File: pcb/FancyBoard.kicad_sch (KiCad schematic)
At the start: 171 parts, among them J1 Conn_01x02_Socket, SW1 SW_Push_45deg, SW10 SW_Push_45deg, SW11 SW_Push_45deg, SW12 SW_Push_45deg, SW13 SW_Push_45deg, SW14 SW_Push_45deg, SW15 SW_Push_45deg, SW16 SW_Push_45deg, SW17 SW_Push_45deg, SW18 SW_Push_45deg, SW19 SW_Push_45deg, SW2 SW_Push_45deg, SW20 SW_Push_45deg, SW21 SW_Push_45deg, SW22 SW_Push_45deg, SW23 SW_Push_45deg, SW24 SW_Push_45deg, SW25 SW_Push_45deg, SW26 SW_Push_45deg, SW27 SW_Push_45deg, SW28 SW_Push_45deg, SW29 SW_Push_45deg, SW3 SW_Push_45deg, SW30 SW_Push_45deg, SW31 SW_Push_45deg, SW32 SW_Push_45deg, SW33 SW_Push_45deg, SW34 SW_Push_45deg, SW35 SW_Push_45deg, SW36 SW_Push_45deg, SW37 SW_Push_45deg, SW38 SW_Push_45deg, SW39 SW_Push_45deg, SW4 SW_Push_45deg, SW40 SW_Push_45deg, SW41 SW_Push_45deg, SW42 SW_Push_45deg, SW43 SW_Push_45deg, SW44 SW_Push_45deg, SW45 SW_Push_45deg, SW46 SW_Push_45deg, SW47 SW_Push_45deg, SW48 SW_Push_45deg, SW49 SW_Push_45deg, SW5 SW_Push_45deg, SW50 SW_Push_45deg, SW51 SW_Push_45deg, SW52 SW_Push_45deg, SW53 SW_Push_45deg, SW54 SW_Push_45deg, SW55 SW_Push_45deg, SW56 RotaryEncoder_Switch, SW57 RotaryEncoder_Switch, SW58 SW_SPDT, SW6 SW_Push_45deg, SW7 SW_Push_45deg, SW70 SW_Push_45deg, SW71 SW_Push_45deg, SW72 SW_Push_45deg, SW73 SW_Push_45deg, SW74 SW_Push_45deg, SW75 SW_Push_45deg, SW76 SW_Push_45deg, SW77 SW_Push_45deg, SW78 SW_Push_45deg, SW79 SW_Push_45deg, SW8 SW_Push_45deg, SW80 SW_Push_45deg, SW81 SW_Push_45deg, SW82 SW_Push_45deg, SW83 SW_Push_45deg, SW84 SW_Push_45deg, SW85 SW_Push_45deg, SW86 SW_Push_45deg, SW87 SW_Push_45deg, SW88 SW_Push_45deg, SW89 SW_Push_45deg, SW9 SW_Push_45deg, SW90 SW_Push_45deg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

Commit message: schematic done
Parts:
- added R10, R11, R6, R7, R8, R9: 10K, symbol Device:R
- added R2, R3, R4, R5: 4.7K, symbol Device:R
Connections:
- net +3V3: now also R1.1, R10.1, R11.1, R2.1, R3.1, R4.1, R5.1, R6.1, R7.1, R8.1, R9.1; no longer SW58.1 (A)
- net GND: now also SW58.2 (B); no longer R1.2, SW58.3 (C), U2.5 (RES)
- net IO15: now also R8.2
- net IO16: now also R1.2, U2.5 (RES); no longer R1.1
- net IO18: now also SW58.1 (A), R10.2, R7.2; no longer SW58.2 (B)
- net IO19: now also R6.2
- net IO20: now also R9.2
- net SCL: now also R3.2, R5.2
- net SDA: now also R2.2, R4.2
- new net IO9: R11.2, SW58.3 (C)
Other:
- moved on the sheet: C1, C2, C5, C6, D1, D10, D11, D12, D13, D14, D15, D16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

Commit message: mostly done pcb
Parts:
- removed D69: 1N4148W, Diode_SMD:D_SOD-123, symbol Diode:1N4148W
- removed SW83, SW93: SW_Push_45deg, symbol Switch:SW_Push_45deg
- added SW78: SW_Push_45deg, Kailh_PG1353_Hotswap:Kailh-PG1353-Hotswap-1U, symbol Switch:SW_Push_45deg
- C1, C2, C5, C6: footprint (none) -> Capacitor_SMD:C_0603_1608Metric
- J1: footprint (none) -> Connector_JST:JST_PH_B2B-PH-K_1x02_P2.00mm_Vertical
- R1, R10, R11, R2, R3, R4, R5, R6, R7, R8, R9: footprint (none) -> Resistor_SMD:R_0603_1608Metric
- SW1, SW14, SW29, SW42: footprint (none) -> Kailh_PG1353_Hotswap:Kailh-PG1353-Hotswap-1.5U
- SW10, SW11, SW12, SW13, SW15, SW16, SW17, SW18, SW19, SW2, SW20, SW21, SW22, SW23, SW24, SW25, SW26, SW27, SW3, SW30, SW31, SW32, SW33, SW34, SW35, SW36, SW37, SW38, SW39, SW4, SW40, SW41, SW44, SW45, SW46, SW47, SW48, SW49, SW5, SW50, SW51, SW52, SW53, SW54, SW6, SW7, SW8, SW9: footprint (none) -> Kailh_PG1353_Hotswap:Kailh-PG1353-Hotswap-1U
- SW28: footprint (none) -> Kailh_PG1353_Hotswap:Kailh-PG1353-Hotswap-2U
- SW43: footprint (none) -> Kailh_PG1353_Hotswap:Kailh-PG1353-Hotswap-1.75U
- SW55: footprint (none) -> Kailh_PG1353_Hotswap:Kailh-PG1353-Hotswap-2.25U
- SW56: renamed from SW70; footprint (none) -> Kailh_PG1353_Hotswap:Kailh-PG1353-Hotswap-2.25U
- SW57: renamed from SW71; footprint (none) -> Kailh_PG1353_Hotswap:Kailh-PG1353-Hotswap-1U
- SW58: renamed from SW72; footprint (none) -> Kailh_PG1353_Hotswap:Kailh-PG1353-Hotswap-1U
- SW59: renamed from SW73; footprint (none) -> Kailh_PG1353_Hotswap:Kailh-PG1353-Hotswap-1U
- SW60: renamed from SW74; footprint (none) -> Kailh_PG1353_Hotswap:Kailh-PG1353-Hotswap-1U
- SW61: renamed from SW75; footprint (none) -> Kailh_PG1353_Hotswap:Kailh-PG1353-Hotswap-1U
- SW62: renamed from SW76; footprint (none) -> Kailh_PG1353_Hotswap:Kailh-PG1353-Hotswap-1U
- SW63: renamed from SW77; footprint (none) -> Kailh_PG1353_Hotswap:Kailh-PG1353-Hotswap-1U
- SW64: renamed from SW78; footprint (none) -> Kailh_PG1353_Hotswap:Kailh-PG1353-Hotswap-1U
- SW65: renamed from SW79; footprint (none) -> Kailh_PG1353_Hotswap:Kailh-PG1353-Hotswap-1U
- SW66: renamed from SW80; footprint (none) -> Kailh_PG1353_Hotswap:Kailh-PG1353-Hotswap-1U
- SW67: renamed from SW81; footprint (none) -> Kailh_PG1353_Hotswap:Kailh-PG1353-Hotswap-1.75U
- SW68: renamed from SW82; footprint (none) -> Kailh_PG1353_Hotswap:Kailh-PG1353-Hotswap-1U
- SW69: renamed from SW84; footprint (none) -> Kailh_PG1353_Hotswap:Kailh-PG1353-Hotswap-1.25U
- SW70: renamed from SW85; footprint (none) -> Kailh_PG1353_Hotswap:Kailh-PG1353-Hotswap-1.25U
- SW71: renamed from SW86; footprint (none) -> Kailh_PG1353_Hotswap:Kailh-PG1353-Hotswap-1.25U
- SW72: renamed from SW87; footprint (none) -> Kailh_PG1353_Hotswap:Kailh-PG1353-Hotswap-6.25U
- SW73: renamed from SW88; footprint (none) -> Kailh_PG1353_Hotswap:Kailh-PG1353-Hotswap-1U
- SW74: renamed from SW89; footprint (none) -> Kailh_PG1353_Hotswap:Kailh-PG1353-Hotswap-1U
- SW75: renamed from SW90; footprint (none) -> Kailh_PG1353_Hotswap:Kailh-PG1353-Hotswap-1U
- SW76: renamed from SW91; footprint (none) -> Kailh_PG1353_Hotswap:Kailh-PG1353-Hotswap-1U
- SW77: renamed from SW92; footprint (none) -> Kailh_PG1353_Hotswap:Kailh-PG1353-Hotswap-1U
- SW93: renamed from SW56; footprint (none) -> Rotary_Encoder:RotaryEncoder_Alps_EC11E-Switch_Vertical_H20mm
- SW94: renamed from SW57; footprint (none) -> Rotary_Encoder:RotaryEncoder_Alps_EC11E-Switch_Vertical_H20mm
- SW95: renamed from SW58; footprint (none) -> SS-12D00:SS12-D00
- U1: footprint (none) -> nice!nanov2:nice!nanov2
- U2: footprint (none) -> ST7789_Module:ST7789_Module
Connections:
- net COL10: now also SW78.1
- net GND: now also U1.1 (GND), U1.22 (3.3V), U1.5 (GND); no longer U1.26 (3.3V)
- net IO14: now also R8.2, SW94.A, U1.16 (IO14); no longer SW93.S1, U1.18 (IO14)
- net IO15: now also R1.2, U1.17 (IO15), U2.5 (RES); no longer R8.2, SW94.A, U1.19 (IO15)
- net IO16: now also SW93.S1, U1.15 (IO16); no longer R1.2, U1.20 (IO16), U2.5 (RES)
- net IO18: now also U1.18 (IO18); no longer U1.22 (IO18)
- net IO19: now also U1.19 (IO19); no longer U1.23 (IO19)
- net IO20: now also U1.20 (IO20); no longer U1.24 (IO20)
- net IO21: now also U1.21 (IO21); no longer U1.25 (IO21)
- net at D79.2 (A): now also SW78.2
- net at J1.1 (Pin_1): now also U1.25 (BATT+); no longer U1.29 (BATT+)
- net at J1.2 (Pin_2): now also U1.24 (GND); no longer U1.28 (GND)
- no-connect marks 17 -> 18

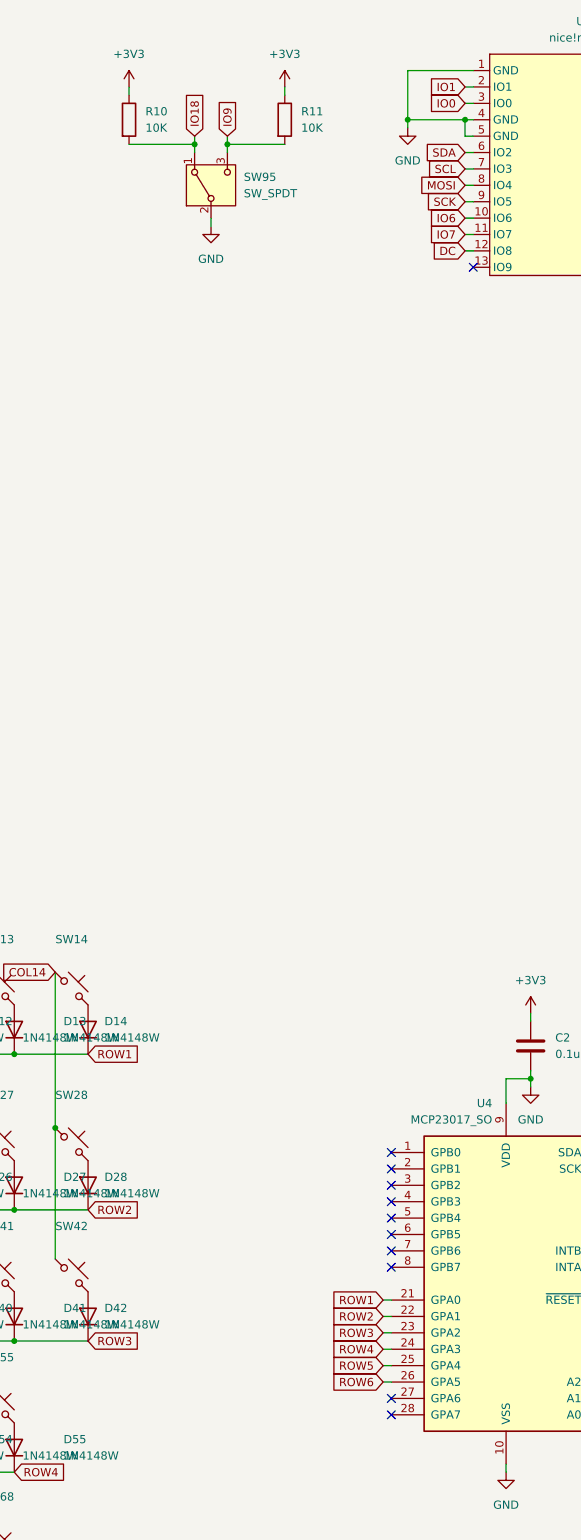
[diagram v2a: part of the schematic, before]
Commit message: mostly done routing
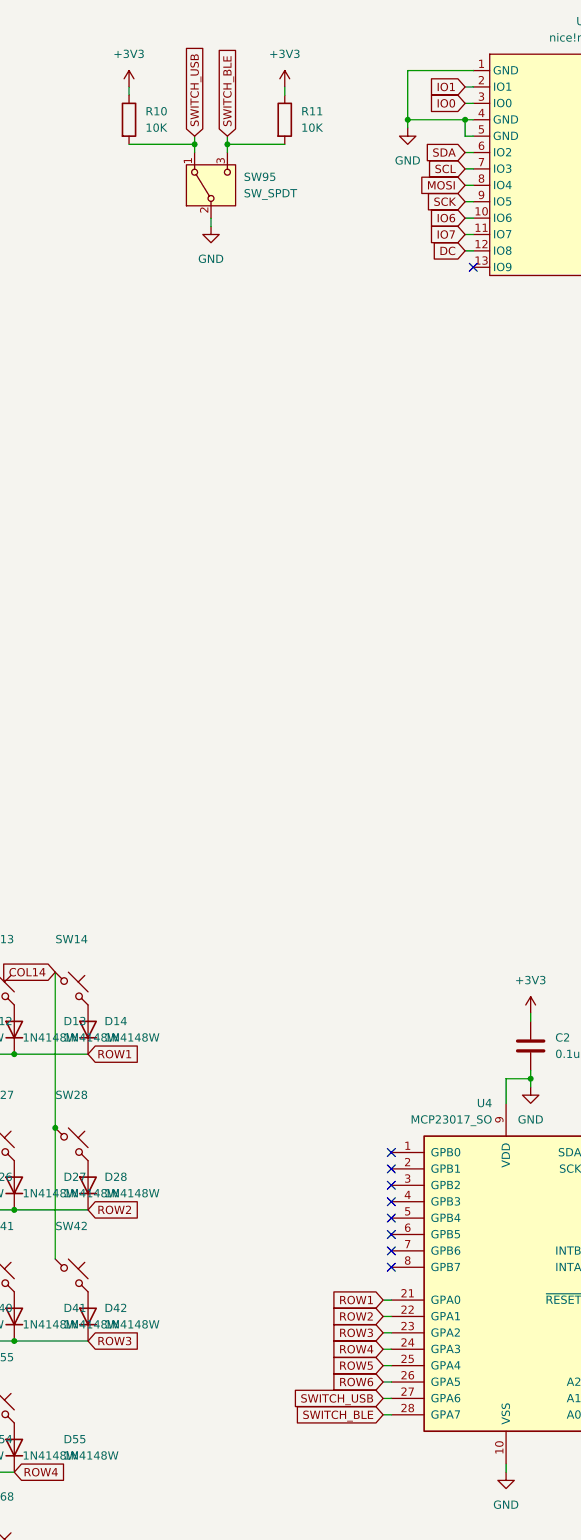
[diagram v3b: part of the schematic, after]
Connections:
- net IO9 is gone; now on net SWITCH_BLE: R11.2, SW95.3 (C)
- net IO18: no longer R10.2, SW95.1 (A)
- net SWITCH_USB: now reaches U4.27 (GPA6)
- net SWITCH_USB: now also R10.2, SW95.1 (A)
- net SWITCH_BLE: now reaches U4.28 (GPA7)
- no-connect marks 18 -> 16
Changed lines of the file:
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@@
 	)
 	(no_connect
-		(at 215.9 231.14)
-	)
-	(no_connect
-		(at 215.9 228.6)
-	)
-	(no_connect
 		(at 215.9 205.74)
 	)
@@
 	(wire
 		(pts
+			(xy 214.63 231.14) (xy 215.9 231.14)
+		)
+		(stroke
+			(width 0)
+			(type default)
+		)
+	)
+	(wire
+		(pts
 			(xy 124.46 175.26) (xy 134.62 175.26)
 		)
@@
 	(wire
 		(pts
+			(xy 262.89 53.34) (xy 264.16 53.34)
+		)
+		(stroke
+			(width 0)
+			(type default)
+		)
+	)
+	(wire
+		(pts
 			(xy 309.88 121.92) (xy 309.88 123.19)
 		)
@@
 	(wire
 		(pts
-			(xy 262.89 53.34) (xy 264.16 53.34)
-		)
-		(stroke
-			(width 0)
-			(type default)
-		)
-	)
-	(wire
-		(pts
 			(xy 328.93 39.37) (xy 328.93 40.64)
 		)
@@
 		)
 	)
+	(wire
+		(pts
+			(xy 214.63 228.6) (xy 215.9 228.6)
+		)
+		(stroke
+			(width 0)
+			(type default)
+		)
+	)
 	(global_label "COL3"
 		(shape input)
@@
 		)
 	)
-	(global_label "IO18"
+	(global_label "SWITCH_USB"
 		(shape input)
 		(at 185.42 33.02 90)
@@
 		)
 		(property "Intersheetrefs" "${INTERSHEET_REFS}"
-			(at 185.42 25.6805 90)
+			(at 185.42 18.4234 90)
 			(effects
 				(font
@@
 		)
 	)
+	(global_label "SWITCH_USB"
+		(shape input)
+		(at 214.63 228.6 180)
+		(fields_autoplaced yes)
+		(effects
+			(font
+				(size 1.27 1.27)
+			)
+			(justify right)
+		)
+		(property "Intersheetrefs" "${INTERSHEET_REFS}"
+			(at 200.0334 228.6 0)
+			(effects
+				(font
+					(size 1.27 1.27)
+				)
+				(justify right)
+				(hide yes)
+			)
+		)
+	)
 	(global_label "ROW5"
 		(shape input)
@@
 		)
 	)
+	(global_label "SWITCH_BLE"
+		(shape input)
+		(at 214.63 231.14 180)
+		(fields_autoplaced yes)
+		(effects
+			(font
+				(size 1.27 1.27)
+			)
+			(justify right)
+		)
+		(property "Intersheetrefs" "${INTERSHEET_REFS}"
+			(at 200.3963 231.14 0)
+			(effects
+				(font
+					(size 1.27 1.27)
+				)
+				(justify right)
+				(hide yes)
+			)
+		)
+	)
 	(global_label "IO0"
 		(shape input)
@@
 		)
 	)
-	(global_label "IO10"
-		(shape input)
-		(at 264.16 53.34 0)
-		(fields_autoplaced yes)
-		(effects
-			(font
-				(size 1.27 1.27)
-			)
-			(justify left)
-		)
-		(property "Intersheetrefs" "${INTERSHEET_REFS}"
-			(at 271.4995 53.34 0)
-			(effects
-				(font
-					(size 1.27 1.27)
-				)
-				(justify left)
-				(hide yes)
-			)
-		)
-	)
-	(global_label "IO9"
+	(global_label "SWITCH_BLE"
 		(shape input)
 		(at 190.5 33.02 90)
@@
 		)
 		(property "Intersheetrefs" "${INTERSHEET_REFS}"
-			(at 190.5 26.89 90)
+			(at 190.5 18.7863 90)
 			(effects
 				(font
@@
 				(hide yes)
 			)
+		)
+	)
+	(global_label "IO10"
+		(shape input)
+		(at 264.16 53.34 0)
+		(fields_autoplaced yes)
+		(effects
+			(font
+				(size 1.27 1.27)
+			)
+			(justify left)
+		)
+		(property "Intersheetrefs" "${INTERSHEET_REFS}"
+			(at 271.4995 53.34 0)
+			(effects
+				(font
+					(size 1.27 1.27)
+				)
+				(justify left)
+				(hide yes)
+			)

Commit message: pcb done?
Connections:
- net +3V3: now also U1.22 (3.3V)
- net GND: no longer U1.22 (3.3V)
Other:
- moved on the sheet: C1
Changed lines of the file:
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@@
 	)
 	(junction
-		(at 281.94 33.02)
-		(diameter 0)
-		(color 0 0 0 0)
-	)
-	(junction
 		(at 107.95 186.69)
 		(diameter 0)
@@
 	)
 	(junction
+		(at 279.4 33.02)
+		(diameter 0)
+		(color 0 0 0 0)
+	)
+	(junction
 		(at 332.74 228.6)
 		(diameter 0)
@@
 	(wire
 		(pts
-			(xy 281.94 33.02) (xy 281.94 31.75)
+			(xy 279.4 33.02) (xy 279.4 31.75)
 		)
 		(stroke
@@
 	(wire
 		(pts
+			(xy 279.4 43.18) (xy 279.4 41.91)
+		)
+		(stroke
+			(width 0)
+			(type default)
+		)
+	)
+	(wire
+		(pts
 			(xy 262.89 38.1) (xy 264.16 38.1)
 		)
@@
 	(wire
 		(pts
-			(xy 281.94 33.02) (xy 281.94 34.29)
+			(xy 279.4 33.02) (xy 279.4 34.29)
 		)
 		(stroke
@@
 	(wire
 		(pts
-			(xy 262.89 33.02) (xy 281.94 33.02)
+			(xy 262.89 33.02) (xy 279.4 33.02)
 		)
 		(stroke
@@
 	(wire
 		(pts
-			(xy 281.94 22.86) (xy 281.94 24.13)
-		)
-		(stroke
-			(width 0)
-			(type default)
-		)
-	)
-	(wire
-		(pts
 			(xy 185.42 33.02) (xy 185.42 34.29)
 		)
@@
 	)
 	(symbol
+		(lib_id "power:+3V3")
+		(at 279.4 31.75 0)
+		(mirror y)
+		(unit 1)
+		(exclude_from_sim no)
+		(in_bom yes)
+		(on_board yes)
+		(dnp no)
+		(property "Reference" "#PWR035"
+			(at 279.4 35.56 0)
+			(effects
+				(font
+					(size 1.27 1.27)
+				)
+				(hide yes)
+			)
+		)
+		(property "Value" "+3V3"
+			(at 279.4 26.67 0)
+			(effects
+				(font
+					(size 1.27 1.27)
+				)
+			)
+		)
+		(property "Footprint" ""
+			(at 279.4 31.75 0)
+			(effects
+				(font
+					(size 1.27 1.27)
+				)
+				(hide yes)
+			)
+		)
+		(property "Datasheet" ""
+			(at 279.4 31.75 0)
+			(effects
+				(font
+					(size 1.27 1.27)
+				)
+				(hide yes)
+			)
+		)
+		(property "Description" "Power symbol creates a global label with name \"+3V3\""
+			(at 279.4 31.75 0)
+			(effects
+				(font
+					(size 1.27 1.27)
+				)
+				(hide yes)
+			)
+		)
+		(pin "1"
+		)
+		(instances
+			(project "FancyBoard"
+				(path "/5df634be-7204-4854-853b-7c7d64057627"
+					(reference "#PWR035")
+					(unit 1)
+				)
+			)
+		)
+	)
+	(symbol
 		(lib_id "Diode:1N4148W")
 		(at 91.44 278.13 90)
@@
 	)
 	(symbol
-		(lib_id "power:+3V3")
-		(at 281.94 22.86 0)
-		(unit 1)
-		(exclude_from_sim no)
-		(in_bom yes)
-		(on_board yes)
-		(dnp no)
-		(property "Reference" "#PWR019"
-			(at 281.94 26.67 0)
-			(effects
-				(font
-					(size 1.27 1.27)
-				)
-				(hide yes)
-			)
-		)
-		(property "Value" "+3V3"
-			(at 281.432 18.796 0)
-			(effects
-				(font
-					(size 1.27 1.27)
-				)
-			)
-		)
-		(property "Footprint" ""
-			(at 281.94 22.86 0)
-			(effects
-				(font
-					(size 1.27 1.27)
-				)
-				(hide yes)
-			)
-		)
-		(property "Datasheet" ""
-			(at 281.94 22.86 0)
-			(effects
-				(font
-					(size 1.27 1.27)
-				)
-				(hide yes)
-			)
-		)
-		(property "Description" "Power symbol creates a global label with name \"+3V3\""
-			(at 281.94 22.86 0)
-			(effects
-				(font
-					(size 1.27 1.27)
-				)
-				(hide yes)
-			)
-		)
-		(pin "1"
-		)
-		(instances
-			(project "FancyBoard"
-				(path "/5df634be-7204-4854-853b-7c7d64057627"
-					(reference "#PWR019")
-					(unit 1)
-				)
-			)
-		)
-	)
-	(symbol
 		(lib_id "Switch:SW_Push_45deg")
 		(at 110.49 229.87 0)
@@
 	)
 	(symbol
-		(lib_id "power:GND")
-		(at 281.94 34.29 0)
-		(unit 1)
-		(exclude_from_sim no)
-		(in_bom yes)
-		(on_board yes)
-		(dnp no)
-		(fields_autoplaced yes)
-		(property "Reference" "#PWR021"
-			(at 281.94 40.64 0)
-			(effects
-				(font
-					(size 1.27 1.27)
-				)
-				(hide yes)
-			)
-		)
-		(property "Value" "GND"
-			(at 281.94 39.37 0)
-			(effects
-				(font
-					(size 1.27 1.27)
-				)
-			)
-		)
-		(property "Footprint" ""
-			(at 281.94 34.29 0)
-			(effects
-				(font
-					(size 1.27 1.27)
-				)
-				(hide yes)
-			)
-		)
-		(property "Datasheet" ""
-			(at 281.94 34.29 0)
-			(effects
-				(font
-					(size 1.27 1.27)
-				)
-				(hide yes)
-			)
-		)
-		(property "Description" "Power symbol creates a global label with name \"GND\" , ground"
-			(at 281.94 34.29 0)
-			(effects
-				(font
-					(size 1.27 1.27)
-				)
-				(hide yes)
-			)
-		)
-		(pin "1"
-		)
-		(instances
-			(project "FancyBoard"
-				(path "/5df634be-7204-4854-853b-7c7d64057627"
-					(reference "#PWR021")
-					(unit 1)
-				)
-			)
-		)
-	)
-	(symbol
 		(lib_id "Diode:1N4148W")
 		(at 58.42 278.13 90)
@@
 	(symbol
 		(lib_id "Device:C")
-		(at 281.94 27.94 0)
+		(at 279.4 38.1 0)
 		(unit 1)
 		(exclude_from_sim no)
@@
 		(fields_autoplaced yes)
 		(property "Reference" "C1"
-			(at 285.75 26.6699 0)
+			(at 283.21 36.8299 0)
 			(effects
 				(font
@@
 		)
 		(property "Value" "10uF"
-			(at 285.75 29.2099 0)
+			(at 283.21 39.3699 0)
 			(effects
 				(font
@@
 		)
 		(property "Footprint" "Capacitor_SMD:C_0603_1608Metric"
-			(at 282.9052 31.75 0)
+			(at 280.3652 41.91 0)
 			(effects
 				(font
@@
 		)
 		(property "Datasheet" "~"
-			(at 281.94 27.94 0)
+			(at 279.4 38.1 0)
 			(effects
 				(font
@@
 		)
 		(property "Description" "Unpolarized capacitor"
-			(at 281.94 27.94 0)
+			(at 279.4 38.1 0)
 			(effects
 				(font
@@
 					(unit 1)
 				)
+			)
+		)
+	)
+	(symbol
+		(lib_id "power:GND")
+		(at 279.4 43.18 0)
+		(unit 1)
+		(exclude_from_sim no)
+		(in_bom yes)
+		(on_board yes)
+		(dnp no)
+		(fields_autoplaced yes)
+		(property "Reference" "#PWR019"
+			(at 279.4 49.53 0)
+			(effects
+				(font
+					(size 1.27 1.27)
+				)
+				(hide yes)
+			)
+		)
+		(property "Value" "GND"
+			(at 279.4 48.26 0)
+			(effects
+				(font
+					(size 1.27 1.27)
+				)
+			)
+		)
+		(property "Footprint" ""
+			(at 279.4 43.18 0)
+			(effects
+				(font
+					(size 1.27 1.27)
+				)
+				(hide yes)
+			)
+		)
+		(property "Datasheet" ""
+			(at 279.4 43.18 0)
+			(effects
+				(font
+					(size 1.27 1.27)
+				)
+				(hide yes)
+			)
+		)
+		(property "Description" "Power symbol creates a global label with name \"GND\" , ground"
+			(at 279.4 43.18 0)
+			(effects
+				(font
+					(size 1.27 1.27)
+				)
+				(hide yes)
+			)
+		)
+		(pin "1"
+		)
+		(instances
+			(project "FancyBoard"
+				(path "/5df634be-7204-4854-853b-7c7d64057627"
+					(reference "#PWR019")
+					(unit 1)
+				)

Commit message: pcb done
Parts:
- SW95: footprint SS-12D00:SS12-D00 -> MSK-12C02:MSK-12C02
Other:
- moved on the sheet: C1, C2, C5, C6, D1, D10, D11, D12, D13, D14, D15, D16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
